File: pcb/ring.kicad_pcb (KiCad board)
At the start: 0 parts

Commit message: pcb
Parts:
- added C1: 100n, Capacitor_SMD:C_0402_1005Metric, F.Cu at (121.3, 99.2)
- added C10: 10u, Capacitor_SMD:C_0603_1608Metric, F.Cu at (117.4, 85.1)
- added C11: 100n, Capacitor_SMD:C_0402_1005Metric, F.Cu at (115.4, 85.1)
- added C2: 4.7u, Capacitor_SMD:C_0603_1608Metric, F.Cu at (107.5, 97.6)
- added C3: 100n, Capacitor_SMD:C_0402_1005Metric, F.Cu at (121.3, 101.2)
- added C4: 10u, Capacitor_SMD:C_0603_1608Metric, F.Cu at (107.5, 99.6)
- added C5: 100nF, Capacitor_SMD:C_0402_1005Metric, F.Cu at (107.5, 101.6)
- added C6: 100n, Capacitor_SMD:C_0402_1005Metric, F.Cu at (107.5, 103.5)
- added C7: 1u, Capacitor_SMD:C_0402_1005Metric, F.Cu at (107.5, 105.5)
- added C8: 4.7u, Capacitor_SMD:C_0603_1608Metric, F.Cu at (112.4, 85.1)
- added C9: 100n, Capacitor_SMD:C_0402_1005Metric, F.Cu at (114.4, 85.1)
- added L1: 2.2u, Capacitor_SMD:C_0603_1608Metric, F.Cu at (124.7, 104.5)
- added MK1: ICS-43434, Sensor_Audio:InvenSense_ICS-43434-6_3.5x2.65mm, B.Cu at (102.6, 87.0)
- added R1: 100k, Resistor_SMD:R_0402_1005Metric, F.Cu at (118.4, 99.2)
- added R2: 10k, Resistor_SMD:R_0402_1005Metric, F.Cu at (118.4, 101.2)
- added R3: 200k, Resistor_SMD:R_0402_1005Metric, F.Cu at (118.4, 103.2)
- added R4: 100k, Resistor_SMD:R_0402_1005Metric, F.Cu at (118.4, 105.2)
- added R5: 10k, Resistor_SMD:R_0402_1005Metric, F.Cu at (118.4, 107.2)
- added U1: TMP117xxDRV, Package_SON:WSON-6-1EP_2x2mm_P0.65mm_EP1x1.6mm, F.Cu at (110.0, 87.4)
- added U2: TLV62569DBV, Package_TO_SOT_SMD:SOT-23-5, F.Cu at (129.5, 87.0)
- added U3: LSM6DSOXTR, Package_LGA:LGA-14_3x2.5mm_P0.5mm_LayoutBorder3x4y, F.Cu at (106.8, 88.2)
- added U4: MAX30102, OptoDevice:Maxim_OLGA-14_3.3x5.6mm_P0.8mm, F.Cu at (114.5, 88.0)
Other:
- board outline added: 32 x 6 mm
- copper layers 0 -> 2

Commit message: schematic basically done
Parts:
- removed C1: 100n, Capacitor_SMD:C_0402_1005Metric
- removed L1: 2.2u, Capacitor_SMD:C_0603_1608Metric
- removed MK1: ICS-43434, Sensor_Audio:InvenSense_ICS-43434-6_3.5x2.65mm
- removed U2: TLV62569DBV, Package_TO_SOT_SMD:SOT-23-5
- added C12: 1.6p, Capacitor_SMD:C_0201_0603Metric, F.Cu at (132.1, 77.2)
- added C13: 18p, Capacitor_SMD:C_0201_0603Metric, F.Cu at (132.1, 79.2)
- added C14: 1u, Capacitor_SMD:C_0402_1005Metric, F.Cu at (132.1, 81.2)
- added C15: C, Capacitor_SMD:C_0201_0603Metric, F.Cu at (136.3, 85.9)
- added C16: C, Capacitor_SMD:C_0201_0603Metric, F.Cu at (136.3, 88.4)
- added C17: 10u, Capacitor_SMD:C_0402_1005Metric, F.Cu at (136.3, 90.9)
- added C18: 100n, Capacitor_SMD:C_0201_0603Metric, F.Cu at (139.8, 85.6)
- added C19: 100n, Capacitor_SMD:C_0201_0603Metric, F.Cu at (139.8, 87.6)
- added C20: 1u, Capacitor_SMD:C_0402_1005Metric, F.Cu at (136.3, 93.4)
- added C21: 10n, Capacitor_SMD:C_0201_0603Metric, F.Cu at (139.8, 89.6)
- added C22: 1u, Capacitor_SMD:C_0402_1005Metric, F.Cu at (136.3, 95.9)
- added C23: 100n, Capacitor_SMD:C_0201_0603Metric, F.Cu at (139.8, 91.5)
- added C24: 100n, Capacitor_SMD:C_0402_1005Metric, F.Cu at (139.8, 93.5)
- added C25: 120p, Capacitor_SMD:C_0402_1005Metric, F.Cu at (142.6, 85.6)
- added C26: 100n, Capacitor_SMD:C_0201_0603Metric, F.Cu at (102.2, 88.0)
- added C29: 1u, Capacitor_SMD:C_0402_1005Metric, F.Cu at (142.6, 87.6)
- added C30: 1u, Capacitor_SMD:C_0402_1005Metric, F.Cu at (142.6, 89.6)
- added C31: 100n, Capacitor_SMD:C_0402_1005Metric, F.Cu at (142.6, 91.5)
- added C32: 120p, Capacitor_SMD:C_0402_1005Metric, F.Cu at (142.6, 93.5)
- added IC1: EFR32BG27C140F768IM32-B, Package_DFN_QFN:QFN-32-1EP_4x4mm_P0.4mm_EP2.9x2.9mm, F.Cu at (123.5, 87.0)
- added MK2: IM69D130, Sensor_Audio:Infineon_PG-LLGA-5-1, F.Cu at (102.4, 85.8)
- added R6: R, Resistor_SMD:R_0201_0603Metric, F.Cu at (141.1, 101.7)
- added U6: TLV62569ADRL, Package_TO_SOT_SMD:SOT-563, F.Cu at (130.3, 88.3)
- C10, C8: footprint Capacitor_SMD:C_0603_1608Metric -> Capacitor_SMD:C_0402_1005Metric
- C11, C6, C9: footprint Capacitor_SMD:C_0402_1005Metric -> Capacitor_SMD:C_0201_0603Metric
- C3: footprint Capacitor_SMD:C_0402_1005Metric -> Resistor_SMD:R_0201_0603Metric
- R1: value 100k -> R; footprint Resistor_SMD:R_0402_1005Metric -> Resistor_SMD:R_0201_0603Metric
- R2, R5: footprint Resistor_SMD:R_0402_1005Metric -> Resistor_SMD:R_0201_0603Metric
- moved R1 22.7 mm to (141.1, 99.9)
- moved U1 9.31 mm to (115.6, 80.0), turned to 180 degrees
- moved U3 9.14 mm to (110.7, 80.0)
- moved C10 7.62 mm to (109.8, 85.4)
- moved C11 6.91 mm to (108.5, 85.2)
- moved U4 6.75 mm to (107.8, 87.8)
- moved C9 6.61 mm to (107.8, 85.2)
- moved C8 5.92 mm to (106.5, 85.4)
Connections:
- net Net-(U1-ALERT) renamed /TMP_INT
- R1 pad 1: /I2S_SD -> /I2C_SCL
- R1 pad 2: GND -> VDD

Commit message: ldo
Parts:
- removed C2: 4.7u, Capacitor_SMD:C_0603_1608Metric
- removed C4: 10u, Capacitor_SMD:C_0603_1608Metric
- removed R3: 200k, Resistor_SMD:R_0402_1005Metric
- removed R4: 100k, Resistor_SMD:R_0402_1005Metric
- removed U6: TLV62569ADRL, Package_TO_SOT_SMD:SOT-563
- added C27: 1u, Capacitor_SMD:C_0402_1005Metric, F.Cu at (127.1, 76.7)
- added C28: 1u, Capacitor_SMD:C_0402_1005Metric, F.Cu at (127.1, 78.7)
- added U2: TPS7A20xxxDQN, Package_SON:Texas_X2SON-4_1x1mm_P0.65mm, F.Cu at (130.0, 86.0)

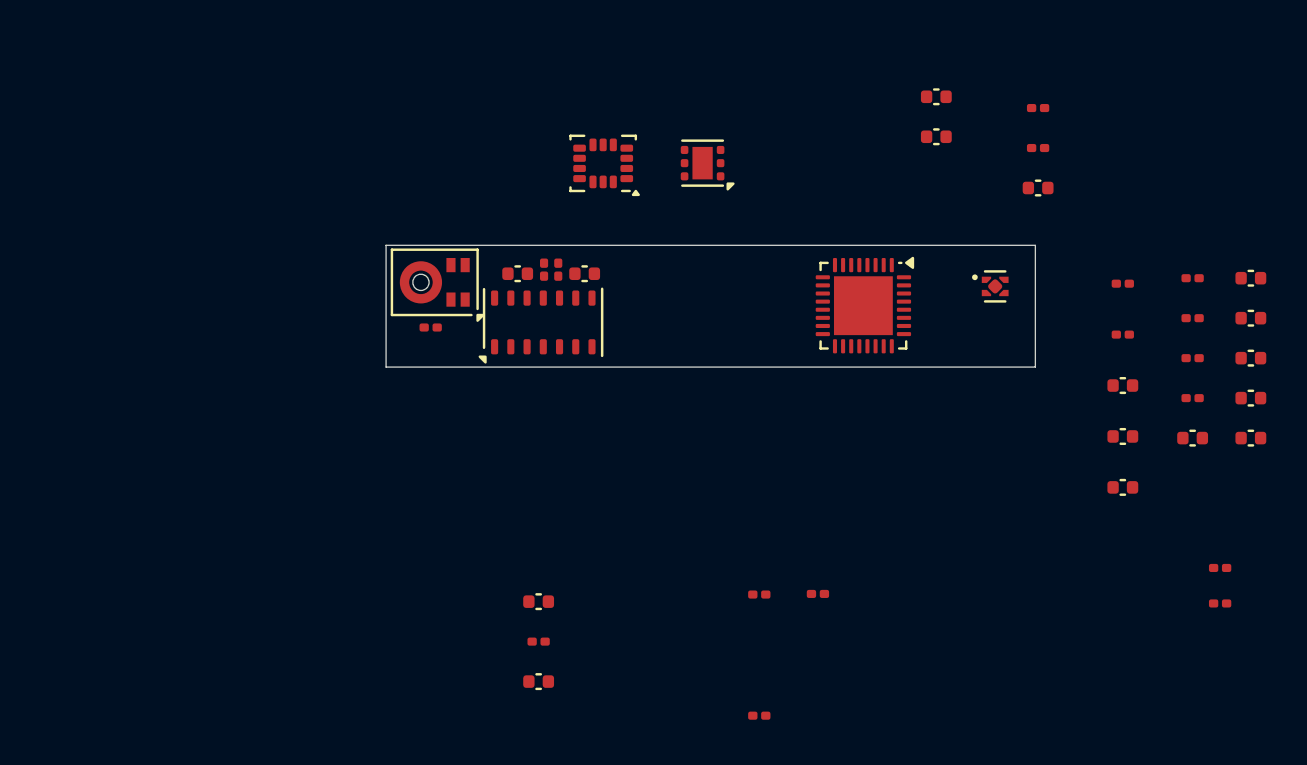
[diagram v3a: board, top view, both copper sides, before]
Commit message: battery protection
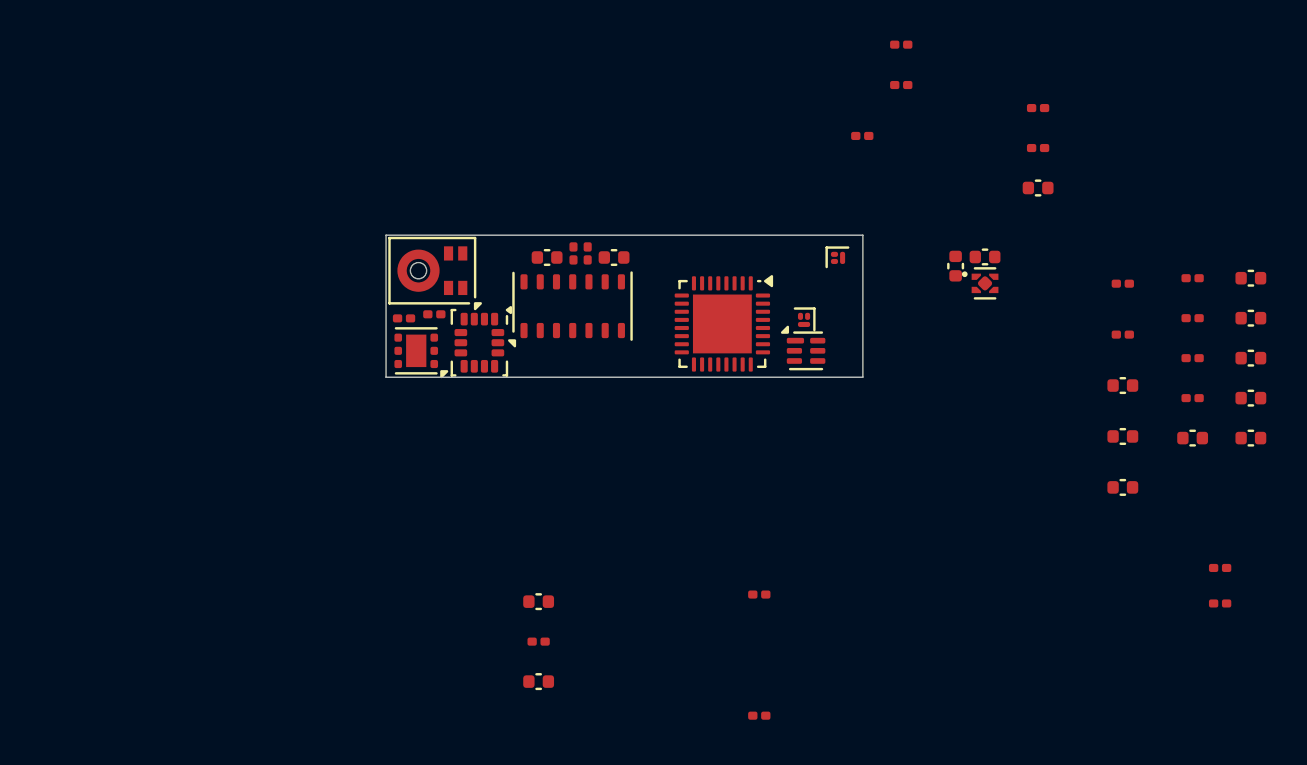
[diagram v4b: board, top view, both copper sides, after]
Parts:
- added C33: 100n, Capacitor_SMD:C_0201_0603Metric, F.Cu at (123.5, 78.6)
- added Q2: CSD13380F3, Package_DFN_QFN:Texas_PicoStar_DFN-3_0.69x0.60mm, F.Cu at (122.3, 84.6)
- added Q3: CSD13380F3, Package_DFN_QFN:Texas_PicoStar_DFN-3_0.69x0.60mm, F.Cu at (120.6, 87.7)
- added R3: 2.2k, Capacitor_SMD:C_0201_0603Metric, F.Cu at (125.4, 74.1)
- added R4: 330, Capacitor_SMD:C_0201_0603Metric, F.Cu at (125.4, 76.1)
- added U5: BQ297xy, Package_SON:WSON-6_1.5x1.5mm_P0.5mm, F.Cu at (120.7, 89.2)
- moved C3 24.5 mm to (100.9, 87.6), turned to 180 degrees
- moved U1 16.9 mm to (101.5, 89.2)
- moved U3 10.7 mm to (104.6, 88.8), turned to -90 degrees
- moved C27 8.25 mm to (129.5, 84.6), turned to 180 degrees
- moved IC1 7.01 mm to (116.6, 87.9)
- moved C28 6.45 mm to (128.1, 85.0), turned to 90 degrees
- moved C10 1.66 mm to (111.2, 84.6)
- moved C8 1.66 mm to (107.9, 84.6)
- moved C11 1.66 mm to (109.9, 84.4)
- moved C9 1.66 mm to (109.2, 84.4)
- moved U4 1.66 mm to (109.2, 87.0)
- moved C26 0.67 mm to (102.4, 87.4)
- moved MK2 0.59 mm to (102.3, 85.2)
- moved U2 0.52 mm to (129.5, 85.9)
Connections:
- IC1 pad 20: unconnected-(IC1-PA03-Pad20) -> /I2C_SCL
- IC1 pad 21: unconnected-(IC1-PA04-Pad21) -> /I2C_SDA
- IC1 pad 31: unconnected-(IC1-PD01-Pad31) -> /MIC_DATA
- IC1 pad 32: unconnected-(IC1-PD00-Pad32) -> /MIC_CLOCK
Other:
- board size 32 x 6 mm -> 23.5 x 7 mm

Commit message: switched to smaller battery, will be removing external protection
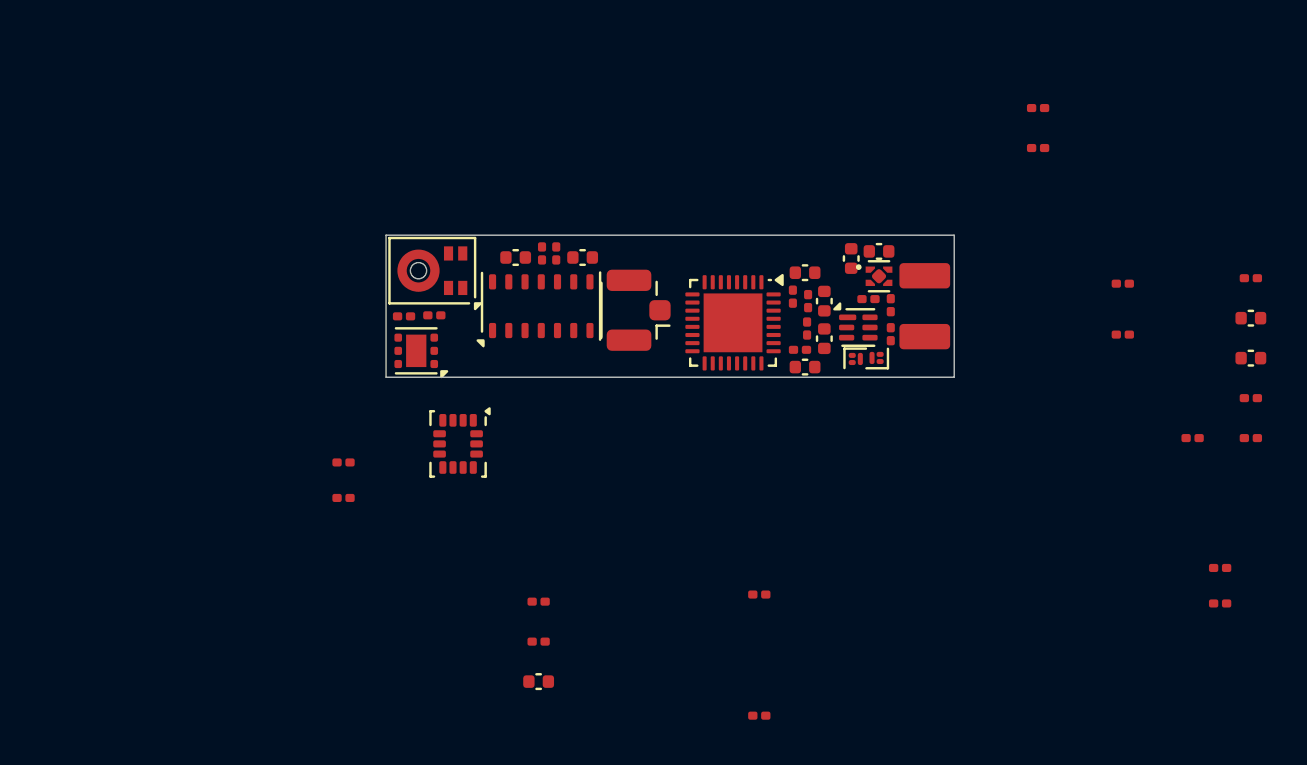
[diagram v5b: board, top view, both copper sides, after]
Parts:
- added BT1: Battery_Cell, library:Battery, F.Cu at (126.5, 87.0)
- added J1: Conn_Coaxial_Small, Connector_Coaxial:U.FL_Hirose_U.FL-R-SMT-1_Vertical, F.Cu at (112.5, 87.2)
- added L2: 2.0n, Inductor_SMD:L_0201_0603Metric, F.Cu at (97.9, 94.7)
- added L3: 3.2n, Inductor_SMD:L_0201_0603Metric, F.Cu at (97.9, 96.5)
- C24, C25, C31, C32, C5: footprint Capacitor_SMD:C_0402_1005Metric -> Capacitor_SMD:C_0201_0603Metric
- moved C23 20.3 mm to (120.0, 86.5), turned to 90 degrees
- moved C19 19.4 mm to (120.4, 89.2)
- moved C18 19.2 mm to (120.8, 88.1), turned to -90 degrees
- moved C21 19.2 mm to (120.8, 86.8), turned to 90 degrees
- moved C22 18.9 mm to (120.7, 85.3), turned to 180 degrees
- moved C20 16.2 mm to (121.6, 86.8), turned to -90 degrees
- moved C17 14.9 mm to (121.6, 88.6), turned to 90 degrees
- moved C14 14.5 mm to (120.7, 90.0), turned to 180 degrees
- moved R3 12.6 mm to (123.8, 86.7), turned to 180 degrees
- moved R4 10.9 mm to (124.9, 87.0), turned to -90 degrees
- moved C33 9.87 mm to (124.9, 88.4), turned to -90 degrees
- moved U2 5.24 mm to (124.3, 85.5)
- moved C27 5.23 mm to (124.3, 84.3)
- moved C28 5.16 mm to (122.9, 84.7)
- moved U3 5.10 mm to (103.5, 93.8)
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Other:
- board size 23.5 x 7 mm -> 28 x 7 mm

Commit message: pcb laid out, schematic done
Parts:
- removed C15, C16: C, Capacitor_SMD:C_0201_0603Metric
- added C34: 1u, Capacitor_SMD:C_0201_0603Metric, F.Cu at (126.7, 86.5)
- added C4: 2.2u, Resistor_SMD:R_0201_0603Metric, F.Cu at (126.7, 85.0)
- added D1: ESD9B5.0ST5G, Diode_SMD:D_SOD-923, F.Cu at (127.3, 89.0)
- added D4: ESD9B3.3ST5G, Diode_SMD:D_SOD-923, F.Cu at (127.5, 86.3)
- added D5: ESD9B3.3ST5G, Diode_SMD:D_SOD-923, F.Cu at (127.5, 84.8)
- added FB1: BLM18AG102SN1, Inductor_SMD:L_0603_1608Metric, F.Cu at (101.5, 86.8)
- added FB2: BLM18AG102SN1, Inductor_SMD:L_0603_1608Metric, F.Cu at (101.5, 89.7)
- added R7: 10k, Resistor_SMD:R_0201_0603Metric, F.Cu at (122.4, 84.4)
- added R8: 100k, Resistor_SMD:R_0201_0603Metric, F.Cu at (106.3, 95.2)
- added TP2: SWDIO, TestPoint:TestPoint_Pad_D1.0mm, F.Cu at (130.0, 84.5)
- added TP3: SWCLK, TestPoint:TestPoint_Pad_D1.0mm, F.Cu at (135.0, 89.5)
- added TP5: +, TestPoint:TestPoint_Pad_D1.5mm, F.Cu at (132.5, 87.0)
- added TP6: -, TestPoint:TestPoint_Pad_D1.0mm, F.Cu at (130.0, 89.5)
- added TP7: -, TestPoint:TestPoint_Pad_D1.0mm, F.Cu at (135.0, 84.5)
- added U6: BQ27427YZFR, Package_BGA:BGA-9_1.6x1.6mm_Layout3x3_P0.5mm, F.Cu at (124.6, 85.3)
- added Y2: 38.4MHz, Crystal:Crystal_SMD_1210-4Pin_1.2x1.0mm, F.Cu at (104.4, 84.4)
- BT1: moved to B.Cu
- J1: footprint Connector_Coaxial:U.FL_Hirose_U.FL-R-SMT-1_Vertical -> RF_Antenna:Texas_SWRA117D_2.4GHz_Right; moved to B.Cu
- R2, R5: value 10k -> 100k
- moved R1 41.4 mm to (99.8, 96.0)
- moved R6 41.4 mm to (99.8, 97.8)
- moved C32 39.3 mm to (103.7, 88.3), turned to 180 degrees
- moved C25 39.2 mm to (103.4, 85.6), turned to 180 degrees
- moved C31 39.0 mm to (103.7, 89.0), turned to 180 degrees
- moved C29 38.7 mm to (103.9, 87.2)
- moved C30 38.7 mm to (103.9, 89.8)
- moved C24 36.8 mm to (103.7, 86.3)
- moved C13 33.0 mm to (100.4, 88.2), turned to -90 degrees
- moved C12 32.7 mm to (101.5, 88.6), turned to 180 degrees
- moved C7 19.0 mm to (118.3, 89.8), turned to 180 degrees
- moved J1 17.1 mm to (95.5, 89.4)
- moved C6 16.8 mm to (117.0, 89.6), turned to -90 degrees
- moved R5 15.3 mm to (106.4, 97.7)
- moved R2 12.9 mm to (106.5, 96.5)
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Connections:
- C5 pad 1: Net-(U3-VDDIO) -> VDD
- IC1 pad 1: unconnected-(IC1-PC00-Pad1) -> /HBT_INT
- IC1 pad 14: /IMU_INT2 -> unconnected-(IC1-PB02-Pad14)
- IC1 pad 15: /IMU_INT1 -> unconnected-(IC1-PB01-Pad15)
- IC1 pad 16: /HBT_INT -> unconnected-(IC1-PB00-Pad16)
- IC1 pad 3: unconnected-(IC1-PC02-Pad3) -> /IMU_INT1
- IC1 pad 31: /MIC_DATA -> /MIC_CLOCK
- IC1 pad 32: /MIC_CLOCK -> /MIC_DATA
- IC1 pad 5: unconnected-(IC1-PC04-Pad5) -> /IMU_INT2
- U3 pad 5: Net-(U3-VDDIO) -> VDD
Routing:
- net Net-(IC1-PAVDD): track 0.00 -> 5.67 mm
- net Net-(IC1-RFVDD): track 0.00 -> 5.21 mm
- net /RF: track 0.00 -> 4.19 mm
- net Net-(C12-Pad1): track 0.00 -> 1.44 mm
- net GND: track 0.00 -> 0.90 mm, vias 0 -> 4
- net VDD: track 0.00 -> 0.83 mm, vias 0 -> 1
- net Net-(C13-Pad1): track 0.00 -> 0.74 mm
- net /TMP_INT: vias 0 -> 1
- net /I2C_SDA: vias 0 -> 1
- net /I2C_SCL: vias 0 -> 1
- added copper zone on B.Cu, net GND
- added copper zone on F.Cu, net GND
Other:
- board size 28 x 7 mm -> 53 x 7 mm

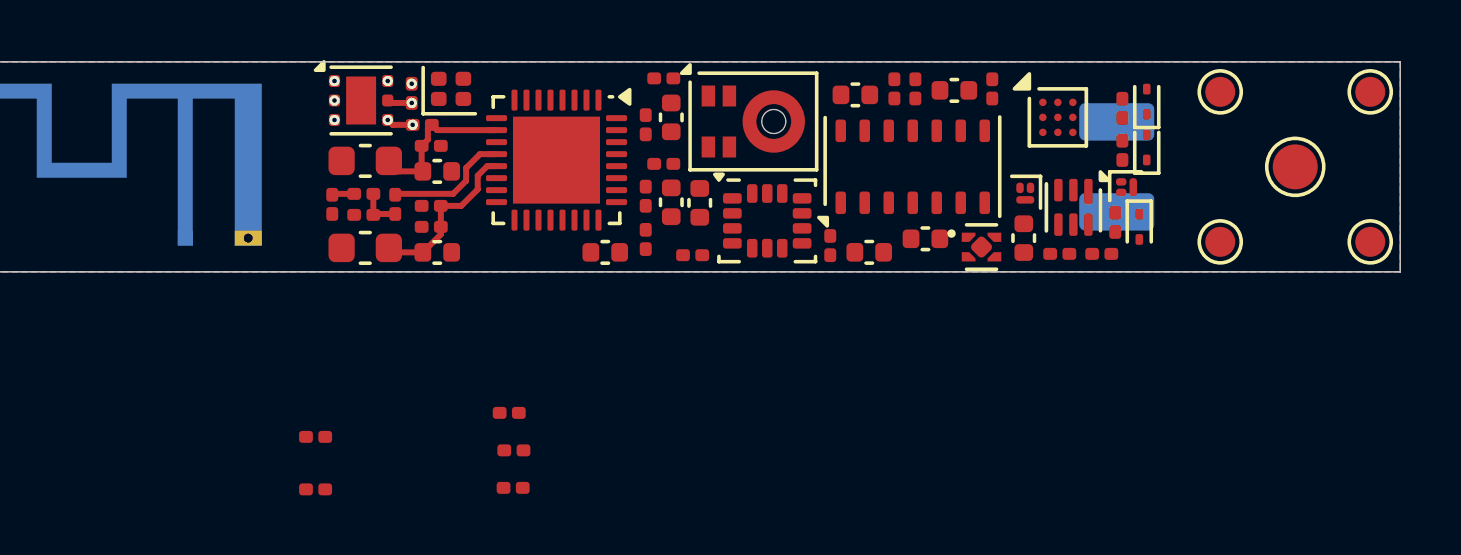
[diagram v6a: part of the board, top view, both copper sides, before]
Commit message: nearly done routing
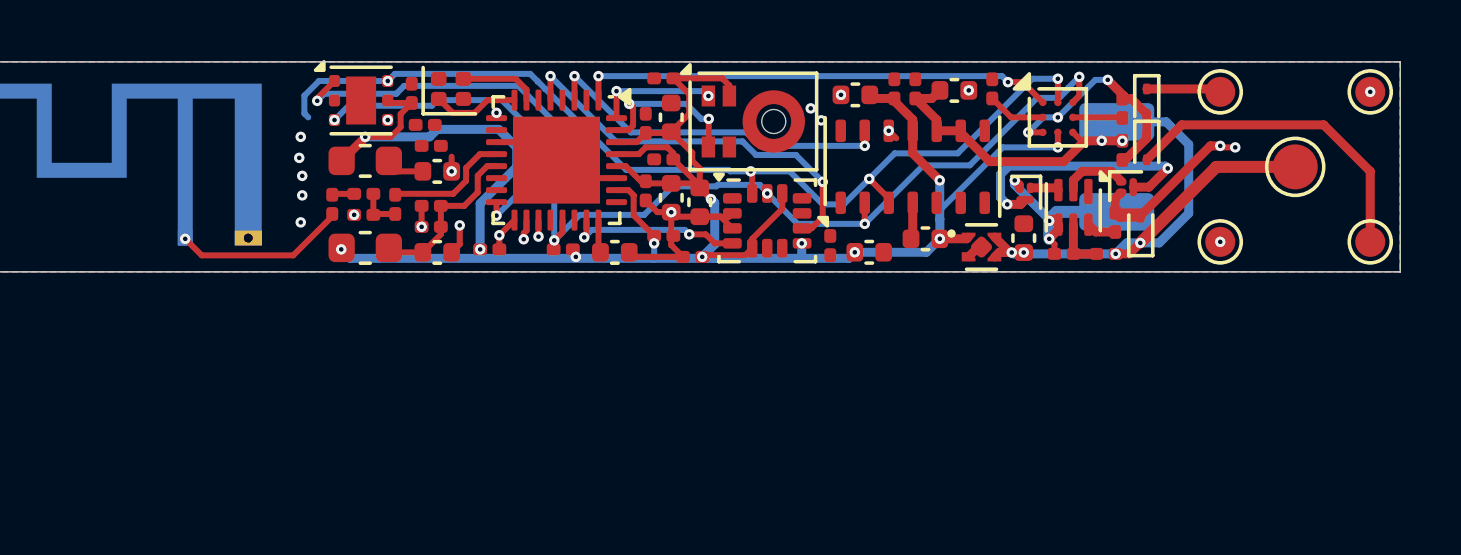
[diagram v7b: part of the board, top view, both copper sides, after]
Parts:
- removed R2, R5, R8: 100k, Resistor_SMD:R_0201_0603Metric
- moved R6 11.5 mm to (108.1, 89.8)
- moved R1 8.53 mm to (105.7, 89.8), turned to 180 degrees
- moved D4 1.53 mm to (127.5, 84.8), turned to -90 degrees
- moved D5 1.52 mm to (127.5, 86.3), turned to -90 degrees
- moved C19 0.61 mm to (111.5, 89.3), turned to 0 degrees
- moved C14 0.32 mm to (109.8, 89.8)
- moved C18 0.18 mm to (110.8, 87.8)
- moved C17 0.15 mm to (111.7, 88.0)
- moved C21 0.15 mm to (111.5, 86.8)
- moved C33 0.14 mm to (124.8, 89.9)
- moved R4 0.14 mm to (126.2, 89.9)
- moved D1 0.11 mm to (127.3, 89.1), turned to 90 degrees
- moved C25 0.10 mm to (103.5, 85.6)
- moved C5 0.06 mm to (112.4, 90.0)
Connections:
- IC1 pad 1: /HBT_INT -> /BAT_LOW
- IC1 pad 16: unconnected-(IC1-PB00-Pad16) -> /TMP_INT
- IC1 pad 17: /TMP_INT -> /I2C_SDA
- IC1 pad 20: /I2C_SCL -> unconnected-(IC1-PA03-Pad20)
- IC1 pad 21: /I2C_SDA -> /I2C_SCL
- IC1 pad 23: unconnected-(IC1-PA06-Pad23) -> /IMU_INT1
- IC1 pad 3: /IMU_INT1 -> /HBT_INT
- R1 pad 1: /I2C_SCL -> /I2C_SDA
- R6 pad 1: /I2C_SDA -> /I2C_SCL
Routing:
- net VDD: track 0.83 -> 73.1 mm, vias 1 -> 12
- net /I2C_SCL: track 0.00 -> 37.1 mm, vias 1 -> 5
- net /I2C_SDA: track 0.00 -> 33.5 mm, vias 1 -> 5
- net +BATT: track 0.00 -> 30.6 mm, vias 0 -> 6
- net GND: track 0.90 -> 31.0 mm, vias 4 -> 23
- net /BAT_LOW: track 0.00 -> 16.0 mm, vias 0 -> 2
- net /IMU_INT2: track 0.00 -> 13.4 mm, vias 0 -> 2
- net /HBT_INT: track 0.00 -> 11.9 mm, vias 0 -> 2
- net Net-(D5-A2): track 0.00 -> 11.6 mm, vias 0 -> 1
- net /TMP_INT: track 0.00 -> 11.1 mm, vias 1 -> 2
- net Net-(Q2-D): track 0.00 -> 8.88 mm, vias 0 -> 2
- net Net-(BT1--): track 0.00 -> 6.59 mm, vias 0 -> 3
- net /IMU_INT1: track 0.00 -> 5.83 mm, vias 0 -> 2
- net Net-(J1-In): track 0.00 -> 5.75 mm, vias 0 -> 1
- net /MIC_CLOCK: track 0.00 -> 5.22 mm, vias 0 -> 2
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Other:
- board text added: "+"
- board text added: "-"
